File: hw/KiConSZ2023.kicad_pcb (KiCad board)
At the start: 4 copper layers, 100 x 70 mm, 257 parts, among them J2 Conn_01x06, J3 USB_C_Receptacle_USB2.0, J4 Conn_02x03_Top_Bottom, J5 Conn_02x03_Top_Bottom, J6 BM20B(0.8)-10DS-0.4V, Q10 2N7002T, Q11 2N7002T, Q12 2N7002T, Q13 2N7002T, Q14 2N7002T, Q15 2N7002T, Q16 2N7002T, Q17 2N7002T, Q18 2N7002T, Q19 2N7002T, Q2 2N7002T, Q20 2N7002T, Q21 2N7002T, Q22 2N7002T, Q23 2N7002T, Q24 2N7002T, Q25 2N7002T, Q26 2N7002T, Q27 2N7002T, Q3 2N7002T, Q4 2N7002T, Q5 2N7002T, Q6 2N7002T, Q7 2N7002T, Q8 2N7002T, Q9 2N7002T, SW2 SKRPACE010, SW3 SKRPACE010, SW4 SW_SPDT, U2 N32L406RBL7, U3 PUSB3FR4, U4 AP3410K, U5 BL8536CB3xx, U6 QMI8658A

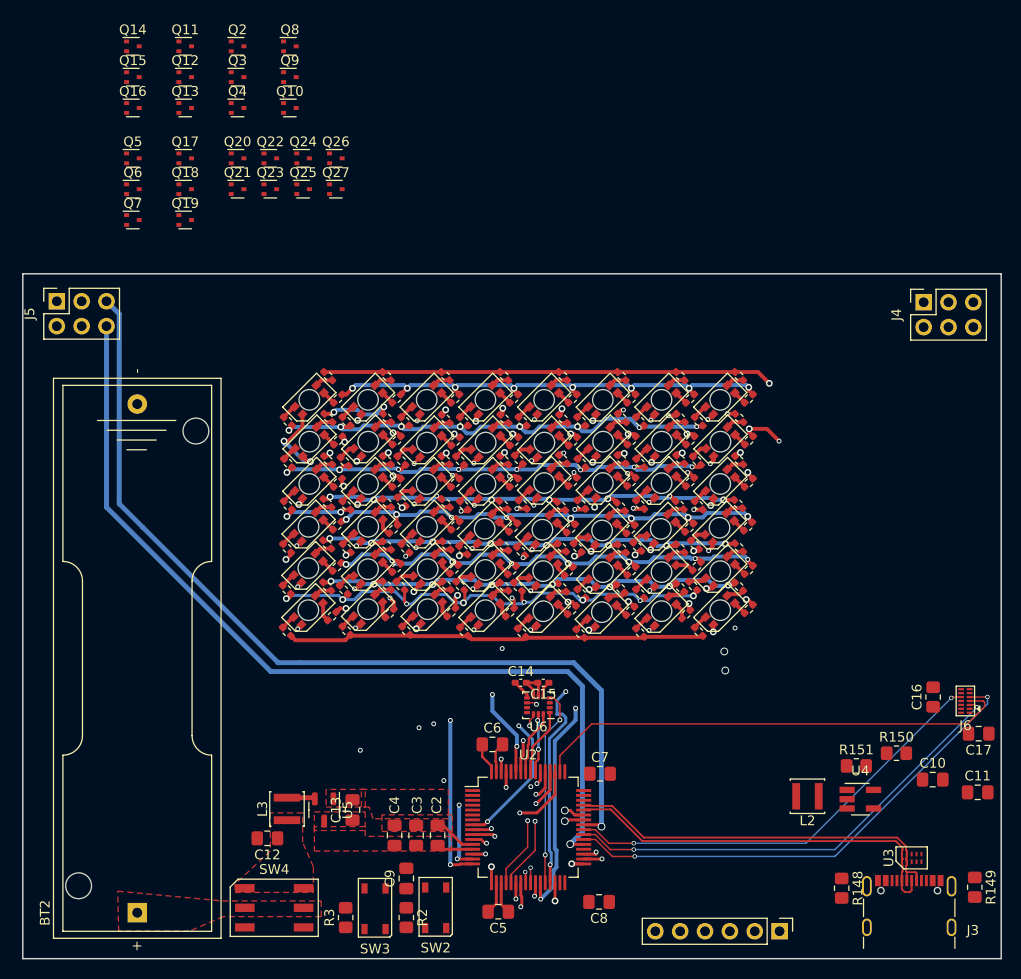
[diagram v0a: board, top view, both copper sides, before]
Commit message: layout and route NMOS
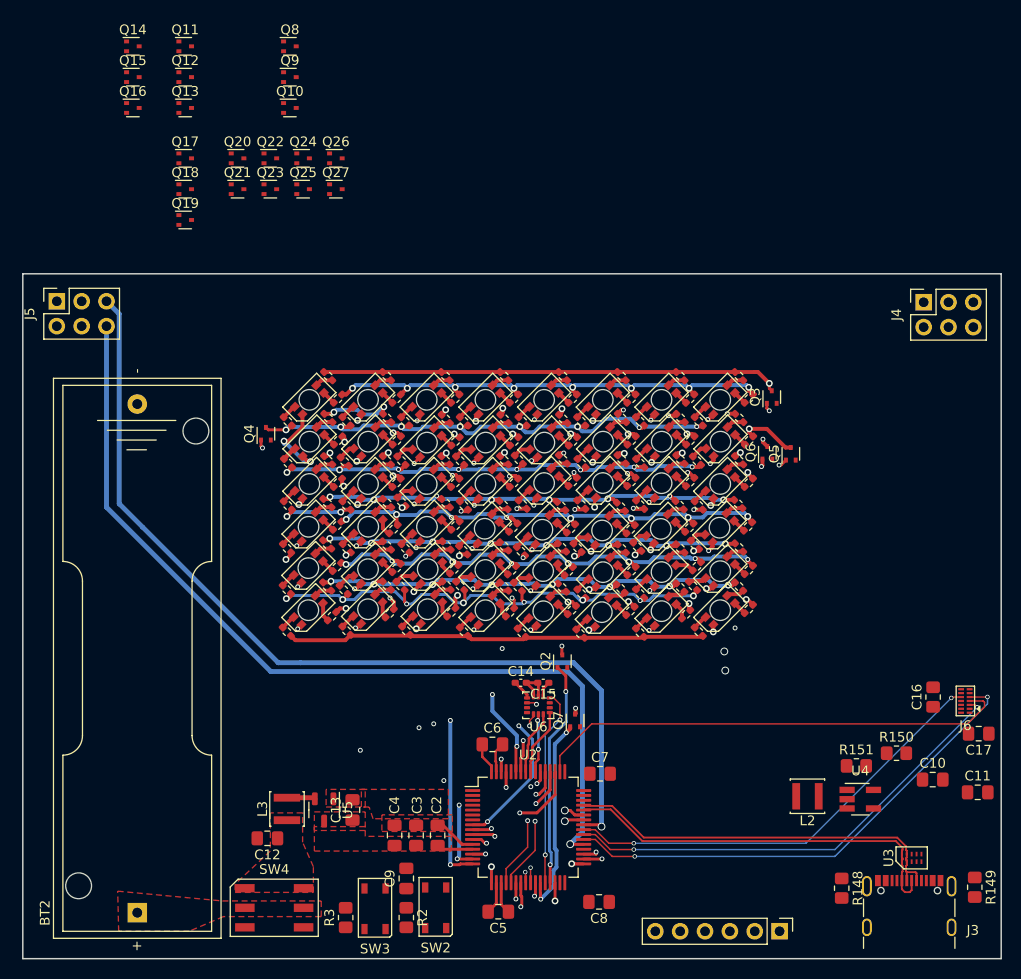
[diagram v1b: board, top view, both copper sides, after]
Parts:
- moved Q5 73.7 mm to (178.5, 98.4), turned to 90 degrees
- moved Q2 71.1 mm to (155.2, 119.6), turned to 90 degrees
- moved Q6 70.2 mm to (176.1, 98.3), turned to 90 degrees
- moved Q7 68.3 mm to (156.4, 125.7), turned to 90 degrees
- moved Q3 63.6 mm to (176.6, 92.6), turned to 90 degrees
- moved Q4 33.4 mm to (124.8, 96.3), turned to 90 degrees
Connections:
- Q20 pad 3: /LED Matrix/VDD -> VDD
- Q21 pad 3: /LED Matrix/VDD -> VDD
- Q22 pad 3: /LED Matrix/VDD -> VDD
- Q23 pad 3: /LED Matrix/VDD -> VDD
- Q24 pad 3: /LED Matrix/VDD -> VDD
- Q25 pad 3: /LED Matrix/VDD -> VDD
- Q26 pad 3: /LED Matrix/VDD -> VDD
- Q27 pad 3: /LED Matrix/VDD -> VDD
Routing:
- net /LowSide_Input_R_Col_1: track 103.3 -> 23.2 mm, vias 10 -> 2
- net /LED Matrix/LED Column 1/LowSide_Input_Source_R: track 0.00 -> 78.0 mm, vias 0 -> 9
- net /LowSide_Input_B_Col_2: track 97.4 -> 20.7 mm, vias 10 -> 2
- net /LED Matrix/LED Column 2/LowSide_Input_Source_B: track 0.00 -> 75.2 mm, vias 0 -> 9
- net /LowSide_Input_R_Col_2: track 127.0 -> 69.7 mm, vias 10 -> 2
- net /LED Matrix/LED Column 2/LowSide_Input_Source_R: track 0.00 -> 57.3 mm, vias 0 -> 8
- net /LowSide_Input_G_Col_2: track 117.1 -> 60.5 mm, vias 9 -> 2
- net /LED Matrix/LED Column 2/LowSide_Input_Source_G: track 0.00 -> 56.1 mm, vias 0 -> 9
- net /LED Matrix/LED Column 1/LowSide_Input_Source_B: track 0.00 -> 53.9 mm, vias 0 -> 8
- net /LowSide_Input_B_Col_1: track 122.5 -> 69.0 mm, vias 9 -> 2
- net /LowSide_Input_G_Col_1: track 117.4 -> 69.4 mm
- net /LED Matrix/LED Column 1/LowSide_Input_Source_G: track 0.00 -> 46.9 mm, vias 0 -> 1

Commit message: layout more nmos
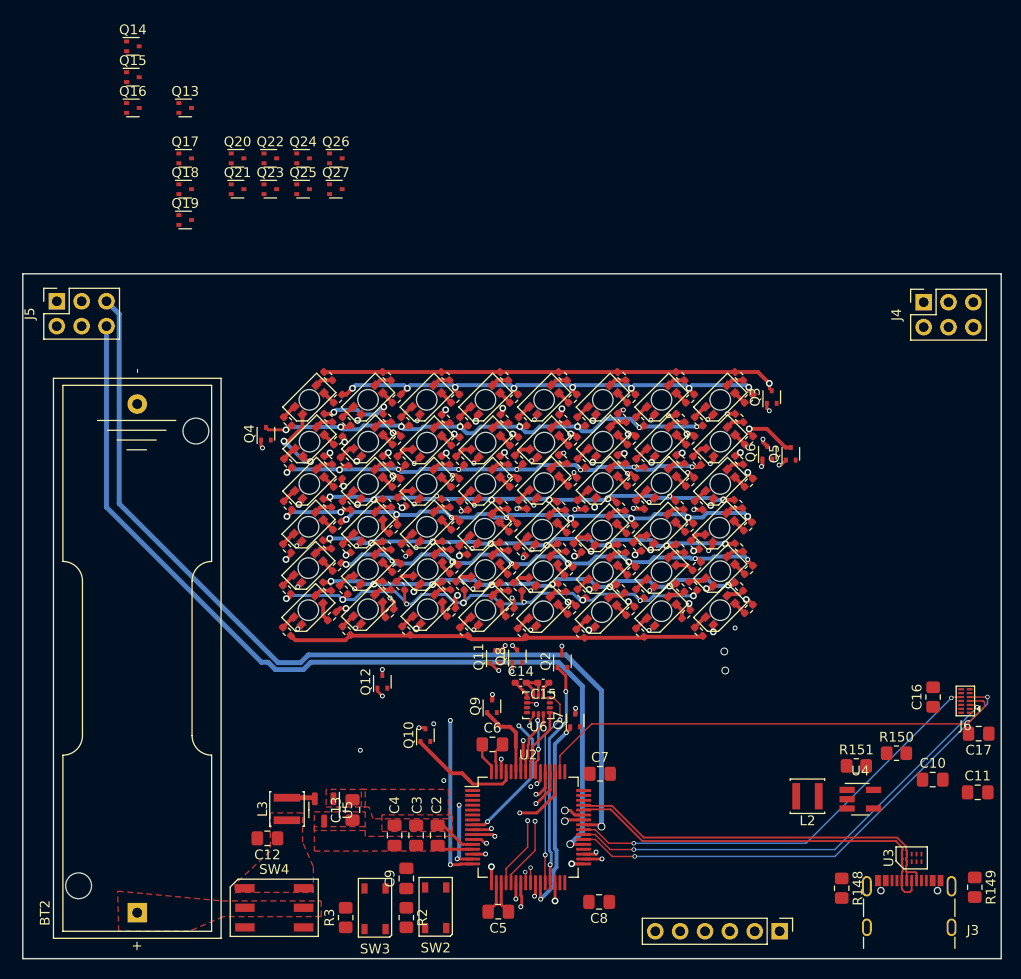
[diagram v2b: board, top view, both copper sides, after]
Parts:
- moved Q11 70.0 mm to (148.3, 119.2), turned to 90 degrees
- moved Q9 67.5 mm to (147.9, 124.2), turned to 90 degrees
- moved Q8 66.5 mm to (150.6, 119.1), turned to 90 degrees
- moved Q10 65.6 mm to (141.2, 127.2), turned to 90 degrees
- moved Q12 65.0 mm to (136.8, 121.7), turned to 90 degrees
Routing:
- net /LowSide_Input_G_Col_3: track 85.2 -> 7.82 mm, vias 10 -> 0
- net /LED Matrix/LED Column 3/LowSide_Input_Source_G: track 0.00 -> 76.8 mm, vias 0 -> 9
- net /LowSide_Input_B_Col_3: track 88.4 -> 11.7 mm, vias 10 -> 0
- net /LED Matrix/LED Column 3/LowSide_Input_Source_B: track 0.00 -> 76.1 mm, vias 0 -> 9
- net /LowSide_Input_R_Col_3: track 84.2 -> 11.7 mm, vias 9 -> 2
- net /LED Matrix/LED Column 3/LowSide_Input_Source_R: track 0.00 -> 71.4 mm, vias 0 -> 9
- net /LowSide_Input_G_Col_4: track 94.4 -> 26.5 mm, vias 10 -> 3
- net /LED Matrix/LED Column 4/LowSide_Input_Source_G: track 0.00 -> 66.8 mm, vias 0 -> 9
- net /LowSide_Input_R_Col_4: track 77.2 -> 11.7 mm, vias 10 -> 2
- net /LED Matrix/LED Column 4/LowSide_Input_Source_R: track 0.00 -> 65.3 mm, vias 0 -> 9
- net /SAO_2_GPIO1: track 94.2 -> 94.9 mm
- net /SAO_2_GPIO2: track 92.8 -> 93.4 mm

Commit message: layout NMOS
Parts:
- moved Q17 79.0 mm to (174.4, 122.0), turned to 90 degrees
- moved Q15 77.9 mm to (159.7, 120.9), turned to 90 degrees
- moved Q14 77.8 mm to (143.7, 127.5), turned to 90 degrees
- moved Q16 76.9 mm to (162.0, 120.8), turned to 90 degrees
- moved Q18 73.2 mm to (172.8, 118.2), turned to 90 degrees
- moved Q19 69.0 mm to (169.1, 119.2), turned to 90 degrees
- moved Q13 68.3 mm to (145.1, 125.1), turned to 90 degrees
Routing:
- net /LowSide_Input_R_Col_5: track 85.0 -> 14.8 mm, vias 10 -> 2
- net /LED Matrix/LED Column 5/LowSide_Input_Source_R: track 0.00 -> 69.2 mm, vias 0 -> 9
- net /LowSide_Input_B_Col_4: track 83.7 -> 15.7 mm, vias 10 -> 2
- net /LED Matrix/LED Column 4/LowSide_Input_Source_B: track 0.00 -> 66.9 mm, vias 0 -> 9
- net /LowSide_Input_G_Col_5: track 91.9 -> 26.3 mm, vias 9 -> 2
- net /LED Matrix/LED Column 5/LowSide_Input_Source_G: track 0.00 -> 63.7 mm, vias 0 -> 9
- net /LowSide_Input_R_Col_6: track 88.6 -> 26.0 mm, vias 9 -> 2
- net /LowSide_Input_B_Col_5: track 85.7 -> 23.5 mm, vias 9 -> 2
- net /LED Matrix/LED Column 6/LowSide_Input_Source_R: track 0.00 -> 62.0 mm, vias 0 -> 8
- net /LED Matrix/LED Column 5/LowSide_Input_Source_B: track 0.00 -> 60.6 mm, vias 0 -> 9
- net /LowSide_Input_G_Col_6: track 84.9 -> 28.8 mm, vias 10 -> 2
- net /LED Matrix/LED Column 6/LowSide_Input_Source_G: track 0.00 -> 56.0 mm, vias 0 -> 9
- net /LowSide_Input_B_Col_6: track 0.00 -> 24.8 mm, vias 0 -> 2
- net /HighSide_Input_Row_8: track 66.6 -> 64.1 mm
- net /LED Matrix/LED Column 6/LowSide_Input_Source_B: track 43.2 -> 44.7 mm
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
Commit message: layout all NMOS
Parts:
- moved Q26 61.6 mm to (164.3, 120.7), turned to 180 degrees
- moved Q27 61.4 mm to (170.4, 119.2), turned to 180 degrees
- moved Q24 56.7 mm to (152.8, 119.5), turned to 180 degrees
- moved Q25 56.3 mm to (157.4, 119.8), turned to 180 degrees
- moved Q22 56.2 mm to (139.6, 122.5), turned to 180 degrees
- moved Q20 54.8 mm to (127.4, 122.7), turned to 180 degrees
- moved Q23 54.4 mm to (145.0, 122.1), turned to 180 degrees
- moved Q21 52.9 mm to (133.4, 123.0), turned to 180 degrees
- moved Q19 1.40 mm to (167.7, 119.2)
- moved Q9 0.15 mm to (147.8, 124.2)
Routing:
- net /HighSide_Input_Row_1: track 75.7 -> 37.2 mm, vias 7 -> 2
- net /LED Matrix/HighSide_Input_Row_Source_1: track 0.00 -> 37.6 mm, vias 0 -> 7
- net /HighSide_Input_Row_2: track 63.8 -> 29.5 mm, vias 8 -> 3
- net /HighSide_Input_Row_3: track 54.2 -> 20.0 mm, vias 8 -> 2
- net /HighSide_Input_Row_4: track 48.8 -> 15.5 mm, vias 7 -> 2
- net /LED Matrix/HighSide_Input_Row_Source_2: track 0.00 -> 33.3 mm, vias 0 -> 7
- net /LED Matrix/HighSide_Input_Row_Source_3: track 0.00 -> 33.2 mm, vias 0 -> 7
- net /HighSide_Input_Row_7: track 61.0 -> 27.9 mm, vias 7 -> 2
- net /LED Matrix/HighSide_Input_Row_Source_4: track 0.00 -> 32.7 mm, vias 0 -> 7
- net /HighSide_Input_Row_5: track 52.6 -> 20.1 mm, vias 8 -> 2
- net /HighSide_Input_Row_6: track 56.9 -> 25.2 mm, vias 7 -> 2
- net /LED Matrix/HighSide_Input_Row_Source_5: track 0.00 -> 31.6 mm, vias 0 -> 7
- net /LED Matrix/HighSide_Input_Row_Source_7: track 0.00 -> 31.4 mm, vias 0 -> 7
- net /LED Matrix/HighSide_Input_Row_Source_8: track 0.00 -> 30.8 mm, vias 0 -> 6
- net /LED Matrix/HighSide_Input_Row_Source_6: track 0.00 -> 30.8 mm, vias 0 -> 7
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
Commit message: routing
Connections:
- J4 pad 2: /GND -> GND
- J5 pad 2: /GND -> GND
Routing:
- net /HighSide_Input_Row_8: track 36.2 -> 35.6 mm
- net /SAO_1_GPIO1: track 74.0 -> 74.1 mm, vias 2 -> 3
- net /SAO_1_GPIO2: track 68.8 -> 68.9 mm, vias 2 -> 3
- net /I2C1_SDA: vias 1 -> 2
- net /I2C1_SCL: vias 1 -> 2
- added copper zone on In2.Cu, net VDD

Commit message: updated
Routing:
- net /LowSide_Input_B_Col_2: track 20.7 -> 24.4 mm
- net /SAO_2_GPIO1: track 94.6 -> 93.9 mm
- net /SAO_2_GPIO2: track 93.4 -> 92.8 mm
- net /LowSide_Input_B_Col_1: track 69.0 -> 69.2 mm, vias 2 -> 4
- net /LowSide_Input_G_Col_2: track 60.5 -> 60.4 mm, vias 2 -> 4
- net /I2C1_SCL: vias 2 -> 1
- net /LowSide_Input_R_Col_2: vias 2 -> 4
- net /LowSide_Input_G_Col_1: vias 2 -> 4
- net /I2C1_SDA: vias 2 -> 1

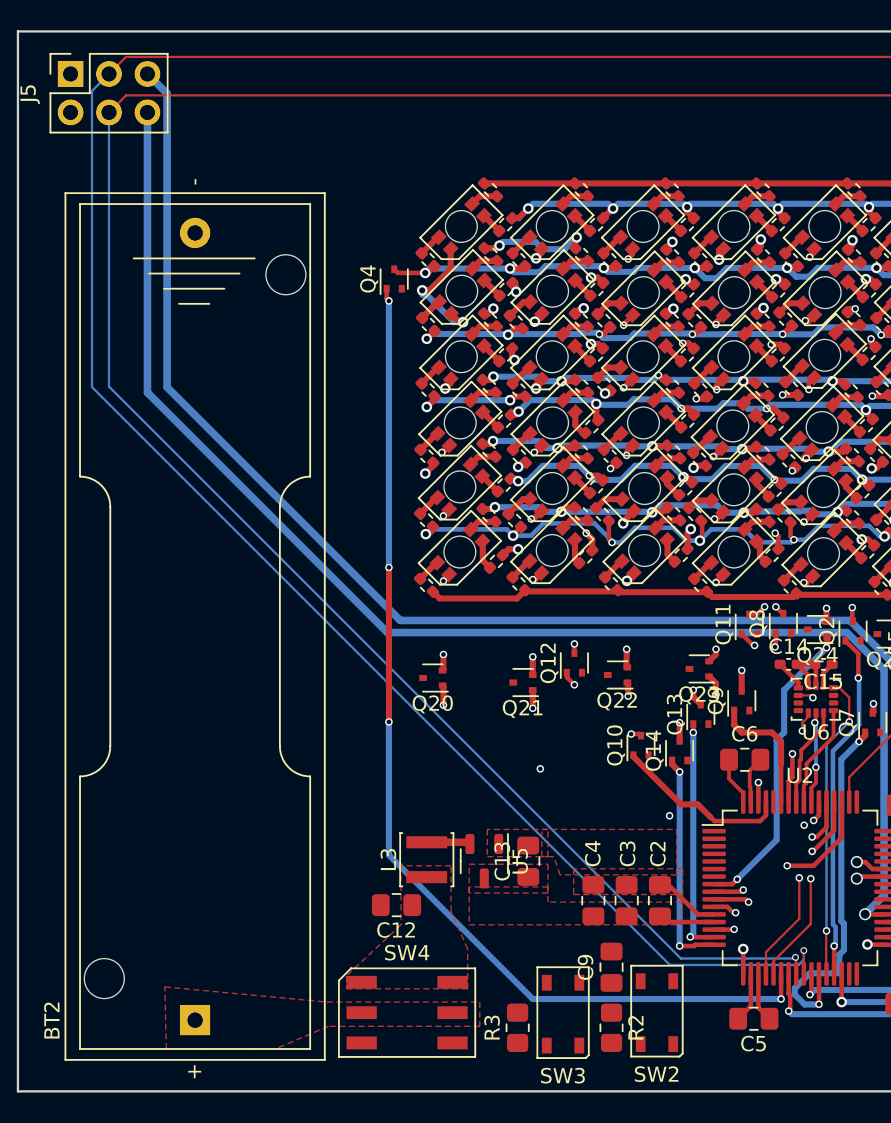
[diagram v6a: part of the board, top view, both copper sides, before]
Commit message: poured Cu
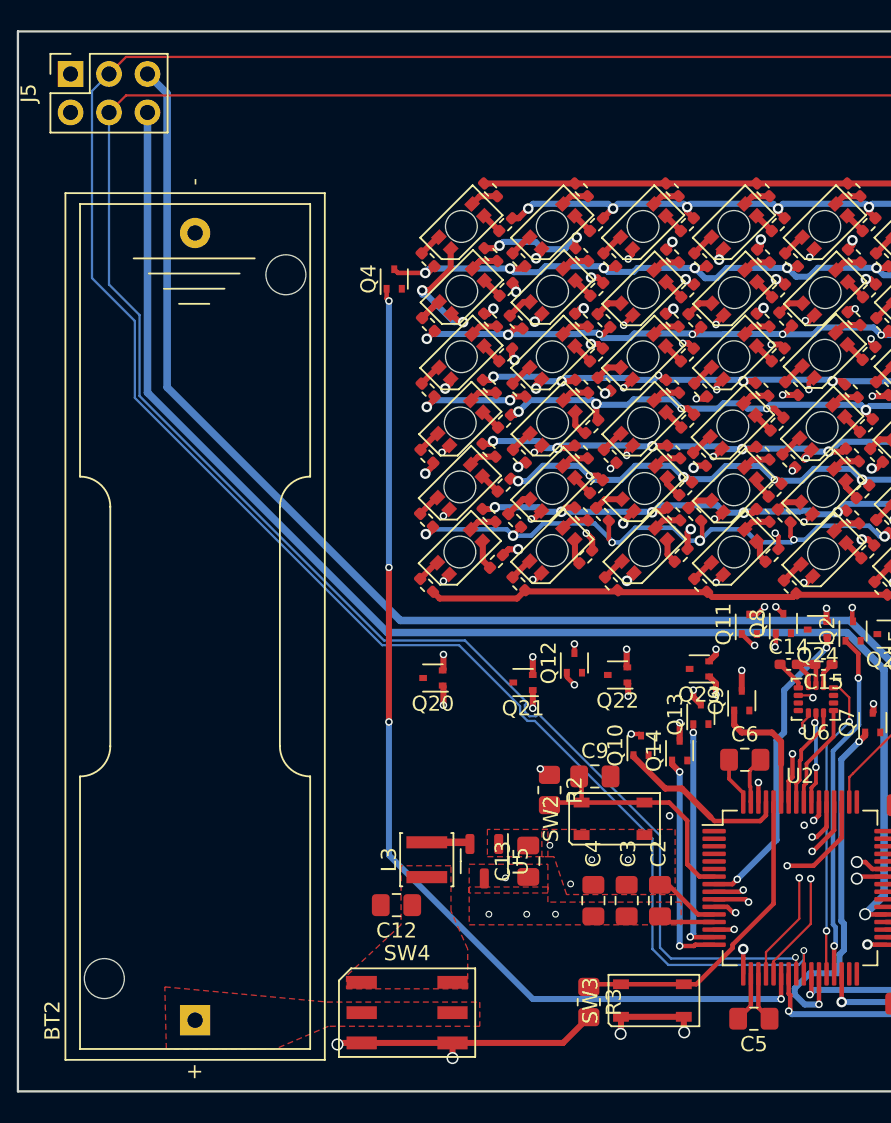
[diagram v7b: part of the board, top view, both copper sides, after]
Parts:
- moved R2 16.2 mm to (135.1, 130.1)
- moved SW2 13.1 mm to (139.3, 132.0), turned to 0 degrees
- moved C9 12.6 mm to (138.1, 129.2), turned to 0 degrees
- moved SW3 5.97 mm to (141.9, 144.0), turned to 0 degrees
- moved R3 5.00 mm to (137.7, 144.1), turned to -90 degrees
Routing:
- net /MCU/BOOT0: track 0.00 -> 21.3 mm
- net GND: track 15.1 -> 33.4 mm, vias 0 -> 6
- net /MCU/~{RST}: track 0.00 -> 16.5 mm
- net VDD: track 13.8 -> 20.2 mm, vias 0 -> 6
- net /I2C1_SCL: track 169.8 -> 174.0 mm
- net /I2C1_SDA: track 175.8 -> 179.1 mm
- net /HighSide_Input_Row_1: track 37.2 -> 35.1 mm

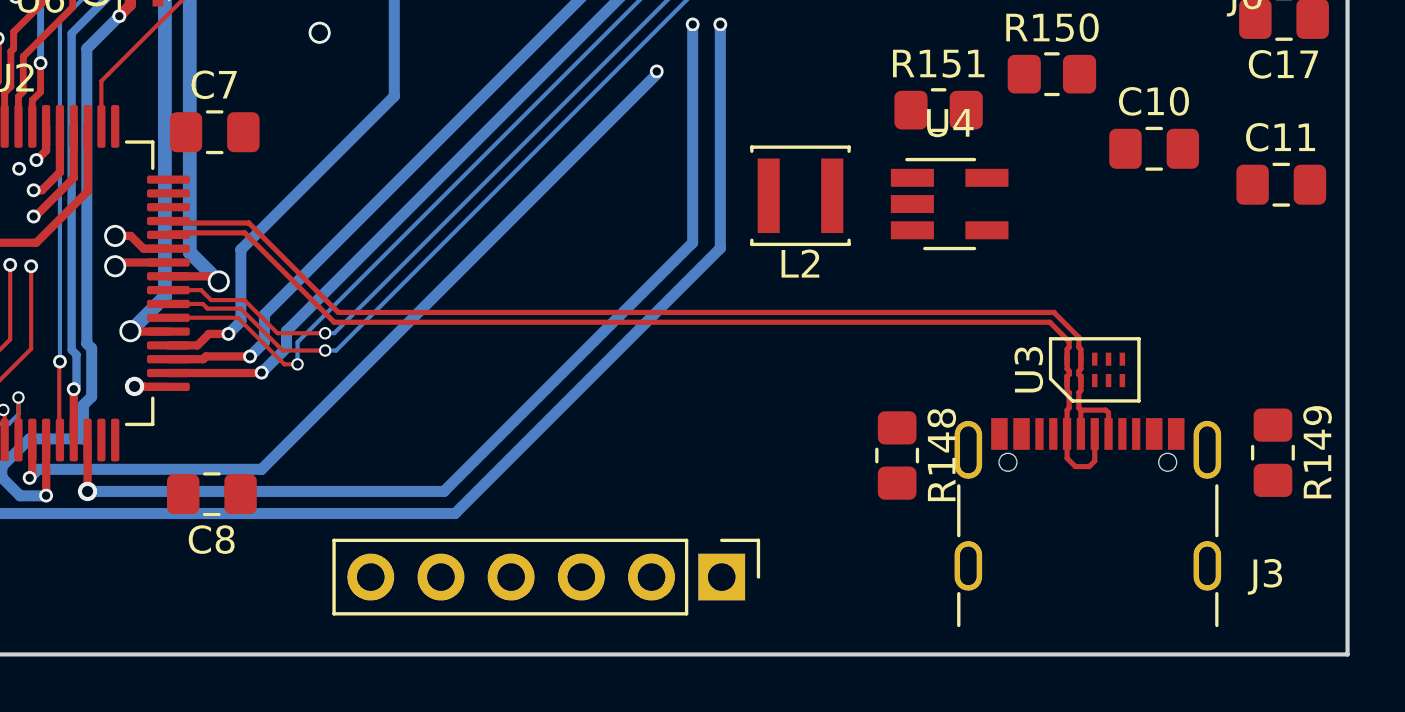
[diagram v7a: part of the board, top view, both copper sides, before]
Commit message: re layout USB Type C
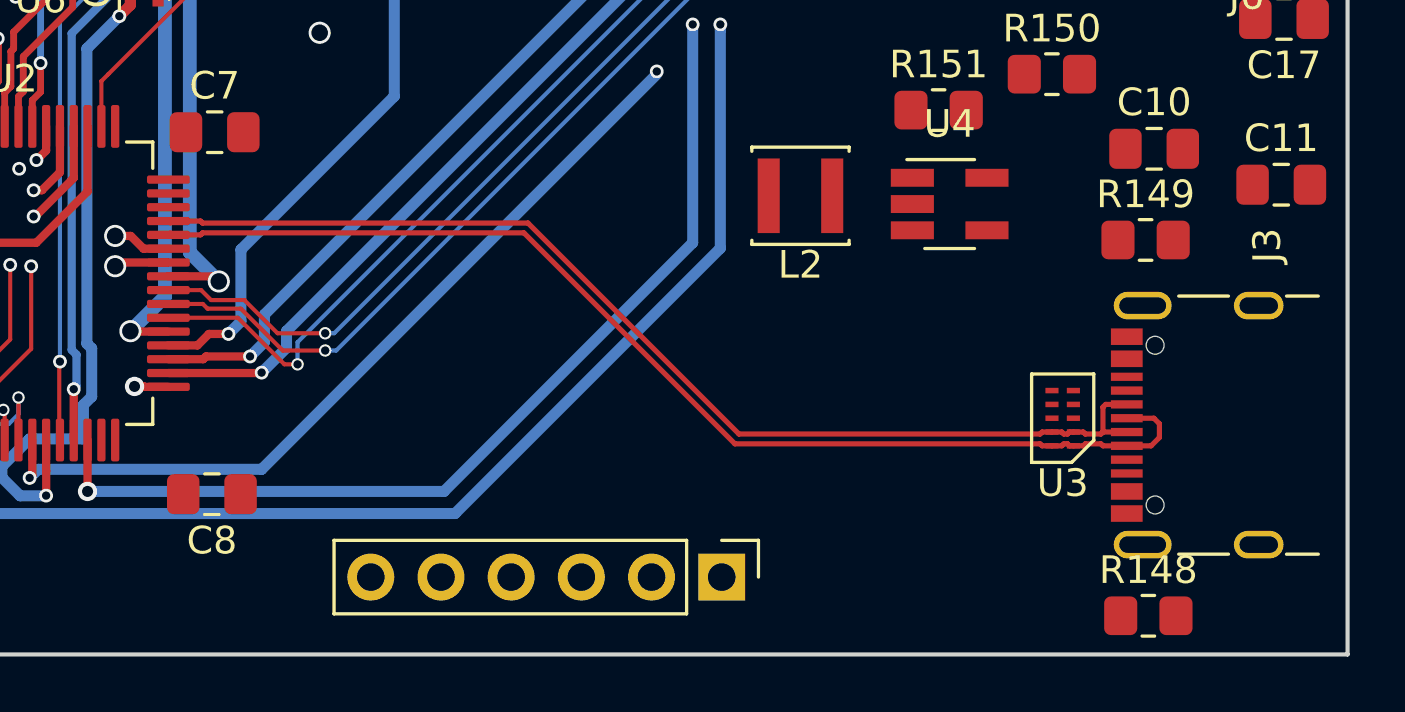
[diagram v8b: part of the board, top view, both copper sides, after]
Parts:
- moved R148 10.8 mm to (192.8, 148.6), turned to 0 degrees
- moved R149 8.97 mm to (192.7, 135.0), turned to 0 degrees
- moved J3 6.47 mm to (195.7, 141.7), turned to 90 degrees
- moved U3 2.10 mm to (189.7, 141.4), turned to 90 degrees
